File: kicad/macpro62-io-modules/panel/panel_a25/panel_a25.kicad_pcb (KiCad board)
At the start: 2 copper layers, 74 x 82.2 mm, 34 parts, among them J1_A1 MOD-A - Hong Cheng HC-USB3.0-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, J1_A2 MOD-A - Hong Cheng HC-USB3.0-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, J1_A3 MOD-A - Hong Cheng HC-USB3.0-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, J1_A4 MOD-A - Hong Cheng HC-USB3.0-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, J2_A1 DF40C-50DP-0.4V(51) C424645 -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, J2_A2 DF40C-50DP-0.4V(51) C424645 -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, J2_A3 DF40C-50DP-0.4V(51) C424645 -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, J2_A4 DF40C-50DP-0.4V(51) C424645 -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, U1_A1 BL24C02F-NTRC (C2828222) 24C0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, U1_A2 BL24C02F-NTRC (C2828222) 24C0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, U1_A3 BL24C02F-NTRC (C2828222) 24C0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, U1_A4 BL24C02F-NTRC (C2828222) 24C0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

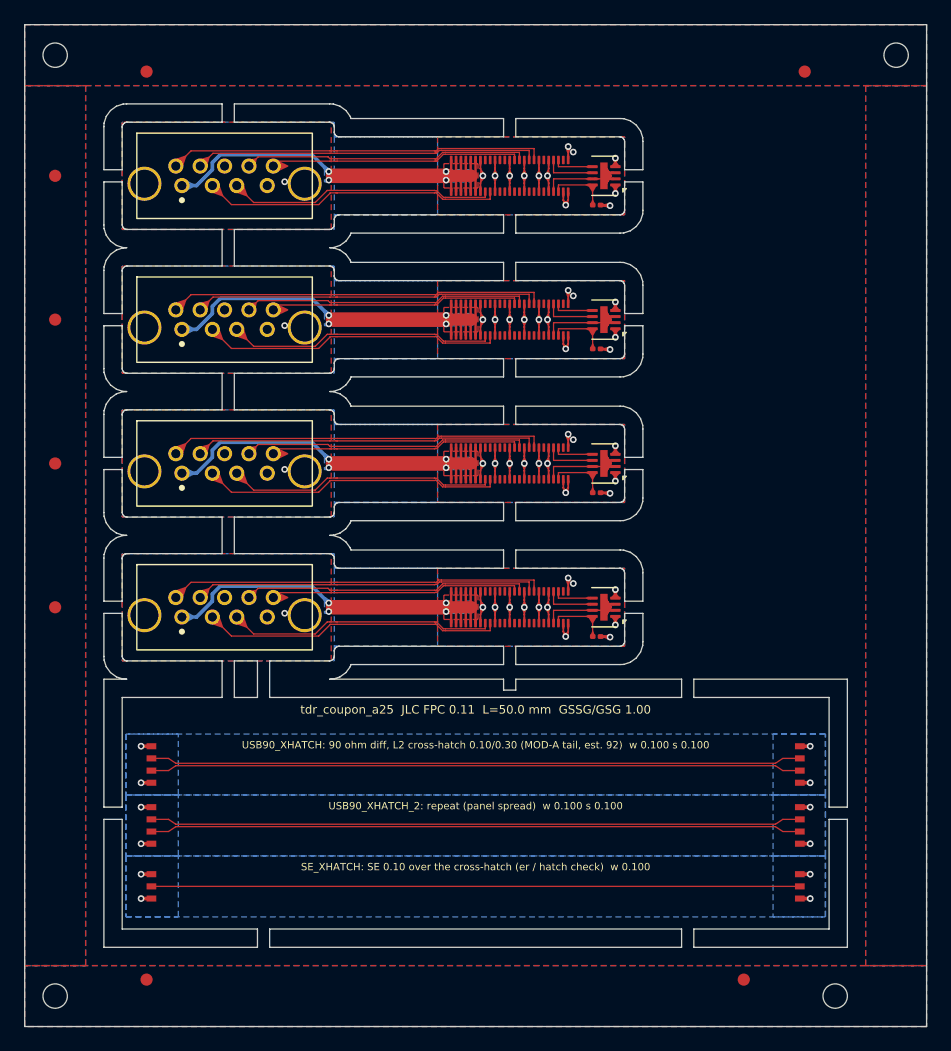
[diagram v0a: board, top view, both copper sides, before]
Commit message: Plate test-print fixes (corners +1mm Y, C2 post -1mm, C1 removed); USB-A/HDMI hand fan-out 0 skew; real DF40 + HDMI footprints
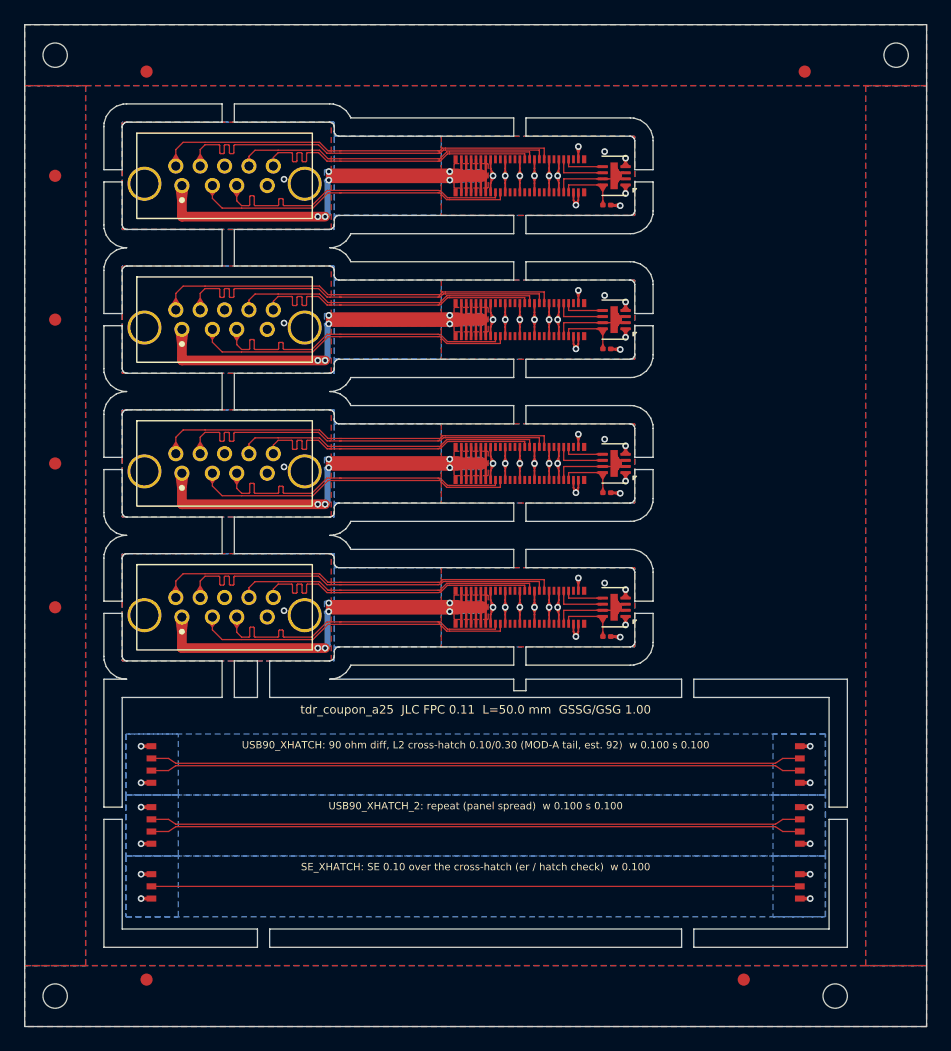
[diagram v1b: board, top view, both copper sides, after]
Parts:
- J2_A1, J2_A2, J2_A3, J2_A4: footprint MP62_MOD:MP62_Hirose_DF40C-50DP-0.4V_PLACEHOLDER -> MP62_MOD:MP62_Hirose_DF40C-50DP-0.4V
- moved C1_A1 0.84 mm to (47.8, 14.8)
- moved C1_A2 0.84 mm to (47.8, 26.6)
- moved C1_A3 0.84 mm to (47.8, 38.4)
- moved C1_A4 0.84 mm to (47.8, 50.2)
- moved J2_A1 0.84 mm to (40.6, 12.4)
- moved J2_A2 0.84 mm to (40.6, 24.2)
- moved J2_A3 0.84 mm to (40.6, 36.0)
- moved J2_A4 0.84 mm to (40.6, 47.8)
- moved U1_A1 0.84 mm to (48.4, 12.4)
- moved U1_A2 0.84 mm to (48.4, 24.2)
- moved U1_A3 0.84 mm to (48.4, 36.0)
- moved U1_A4 0.84 mm to (48.4, 47.8)
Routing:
- net A4/SSTX_N: track 28.3 -> 33.1 mm
- net A2/SSTX_N: track 28.3 -> 33.1 mm
- net A1/SSTX_N: track 28.3 -> 33.1 mm
- net A3/SSTX_N: track 28.3 -> 33.1 mm
- net A1/VBUS: track 42.0 -> 46.8 mm, vias 4 -> 6
- net A3/VBUS: track 42.0 -> 46.8 mm, vias 4 -> 6
- net A2/VBUS: track 42.0 -> 46.8 mm, vias 4 -> 6
- net A4/VBUS: track 42.0 -> 46.8 mm, vias 4 -> 6
- net A3/SSRX_N: track 20.7 -> 25.2 mm
- net A1/SSRX_N: track 20.7 -> 25.2 mm
- net A2/SSRX_N: track 20.7 -> 25.2 mm
- net A4/SSRX_N: track 20.7 -> 25.2 mm
- net A3/D_P: track 22.1 -> 26.4 mm
- net A2/D_P: track 22.1 -> 26.4 mm
- net A1/D_P: track 22.1 -> 26.4 mm
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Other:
- outline, holes or cut-outs redrawn
